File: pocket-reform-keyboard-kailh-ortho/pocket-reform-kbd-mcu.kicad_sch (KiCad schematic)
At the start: 177 parts, among them J1 Conn_01x06_Female, J2 USB, J3 UART, J4 AUX, SW65 SW_HWB, SW66 SW_RST, U1 SN74LV1T34DCK, U2 RP2040, U3 W25Q32JVSS, U4 MCP1700-3302E_SOT23, Y1 12MHz 18pF

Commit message: pocket keyboard 1.1 schematic and pcb mostly done
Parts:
- removed C15, C16, C17, C18, C19, C20, C21, C22, C23, C24, C25, C26, C27, C28, C29, C30, C31, C32, C33, C34, C35, C36, C37, C38, C39, C40, C41, C42, C43, C44, C45, C46, C47, C48, C49, C50, C51, C52, C53, C54, C55, C56, C57, C58, C59, C60, C61, C62, C63, C64, C65, C66, C67, C68, C69, C70, C71, C72, C73, C74, C76, C77, C78, C79: 0.1uF, Capacitor_SMD:C_0603_1608Metric, symbol Device:C_Small
- removed D100, D101, D102, D103, D104, D105, D106, D107, D108, D109, D110, D111, D112, D113, D114, D115, D116, D117, D118, D119, D120, D125, D126, D127, D128, D62, D63, D64, D65, D66, D67, D68, D69, D70, D71, D72, D73, D74, D75, D76, D77, D78, D79, D80, D81, D82, D83, D84, D85, D86, D87, D88, D89, D90, D91, D92, D93, D94, D95, D96, D97, D98, D99: SK6805-EC15, footprints:SK6805-EC15, symbol pocket-reform-keyboard:SK6805-EC15
- removed D61: SK6805-EC15, footprints:SK6805-EC15, symbol LED:SK6805
- removed R8: DNP, Resistor_SMD:R_0603_1608Metric, symbol Device:R_Small
- removed TP1, TP2: TestPoint, TestPoint:TestPoint_Pad_D1.0mm, symbol Connector:TestPoint
- removed U1: SN74LV1T34DCK, Package_TO_SOT_SMD:SOT-353_SC-70-5, symbol Logic_LevelTranslator:SN74LV1T34DCK
- removed U4: MCP1700-3302E_SOT23, Package_TO_SOT_SMD:SOT-23, symbol Regulator_Linear:MCP1700-3302E_SOT23
- added C80, C82: 10uF, Capacitor_SMD:C_0603_1608Metric, symbol Device:C_Small
- added J61: UART, Connector_JST:JST_SH_SM04B-SRSS-TB_1x04-1MP_P1.00mm_Horizontal, symbol Connector_Generic:Conn_01x04
- C1, C10, C11, C14, C2, C3, C4, C5, C6, C8, C9: footprint Capacitor_SMD:C_0603_1608Metric -> Capacitor_SMD:C_0402_1005Metric
- C12, C13: value 27pF -> 15pF; footprint Capacitor_SMD:C_0603_1608Metric -> Capacitor_SMD:C_0402_1005Metric; LCSC C107045 -> (none); Manufacturer Yageo -> (none); Manufacturer_No CC0603JRNPO9BN270 -> (none)
- C7, C75: footprint Capacitor_SMD:C_0603_1608Metric -> Capacitor_SMD:C_0402_1005Metric; LCSC C14664 -> (none); Manufacturer Yageo -> (none); Manufacturer_No CC0603KRX5R8BB105 -> (none)
- R1, R2, R3, R4, R6, R7, R9: footprint Resistor_SMD:R_0603_1608Metric -> Resistor_SMD:R_0402_1005Metric
- R5: value 4.7k -> 1k; footprint Resistor_SMD:R_0603_1608Metric -> Resistor_SMD:R_0402_1005Metric; LCSC C105428 -> (none); Manufacturer_No RC0603FR-074K7L -> (none)
- Y1: value 12MHz 18pF -> 12MHz 12pF; LCSC C91749 -> C20625731; Manufacturer Seiko Epson -> Abracon; Manufacturer_No Q22FA23V0041800 -> ABM8-272-T3
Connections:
- net +1V1: now also C75.1
- net +3V3: now also C80.1, J61.1 (Pin_1)
- net +5V: now also C82.1; no longer C75.1
- net GND: now also C80.2, C82.2, J61.3 (Pin_3)
- net SWC: now also J61.2 (Pin_2)
- net SWD: now also J61.4 (Pin_4)
- no-connect marks 10 -> 9
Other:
- note added: "SWD Debug"
- note added: "changed to 1k!"
- note added: "close to VREG_IN"
- note added: "close to VREG_OUT"
- note removed: "DNP!"
- note removed: "TODO: LCSC: wrong pn! was 4k7"
- note removed: "TODO: check wakeup IRQs"
- moved on the sheet: C1, C10, C11, C12, C13, C14, C2, C3, C4, C5, C6, C7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

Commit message: PREF keyboard: V1.5-R1
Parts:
- added C83: 10uF, Capacitor_SMD:C_0603_1608Metric, symbol Device:C_Small
- added R61, R68: 10k, Resistor_SMD:R_0402_1005Metric, symbol Device:R_Small
- added U12: AP22815A, Package_TO_SOT_SMD:SOT-23-5, symbol reform2:AP22815
- C1, C10, C11, C14, C2, C3, C4, C5, C6, C8, C9: LCSC C14663 -> C1525; Manufacturer Yageo -> Samsung; Manufacturer_No CC0603JPX7R9BB104 -> CL05B104KO5NNNC
- C12, C13: LCSC (none) -> C161530; Manufacturer (none) -> Murata; Manufacturer_No (none) -> GRM1555C1H150FA01D
- C7, C75: LCSC (none) -> C52923; Manufacturer (none) -> Samsung; Manufacturer_No (none) -> CL05A105KA5NQNC
- C80, C82: LCSC (none) -> C19702; Manufacturer (none) -> Samsung; Manufacturer_No (none) -> CL10A106KP8NNNC
- GFX1, H1, H10, H2, H3, H4, H5, H6, H7, H8, H9: now not fitted
- GFX2: footprint footprints:mpre-keyboard-badge-r1 -> footprints:pref-keyboard15-badge; now not fitted
- R1, R2: LCSC C185346 -> C31439; Manufacturer Yageo -> Uni-Royal; Manufacturer_No RC0603FR-0727R4L -> 0402WGF274JTCE
- R3: LCSC C14676 -> C11702; Manufacturer Yageo -> Uni-Royal; Manufacturer_No RC0603JR-071KL -> 0402WGF1001TCE
- R4, R6: LCSC C99198 -> C25744; Manufacturer Yageo -> Uni-Royal; Manufacturer_No RC0603JR-0710KL -> 0402WGF1002TCE
- R5: LCSC (none) -> C11702; Manufacturer Yageo -> Uni-Royal; Manufacturer_No (none) -> 0402WGF1001TCE
- R7, R9: LCSC C105428 -> C25900; Manufacturer Yageo -> Uni-Royal; Manufacturer_No RC0603FR-074K7L -> 0402WGF4701TCE
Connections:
- net +5V: now also R68.2, U12.5 (IN)
- net GND: now also C83.2, R61.1, U12.2 (GND)
- net LED_PWR_EN: now reaches U2.37 (GPIO25)
- net LED_PWR_EN: now also R61.2, U12.4 (EN)
- new net: R68.1, U12.3 (FLG)
- new net LED_POWER: C83.1, U12.1 (OUT)
- no-connect marks 9 -> 8
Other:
- note added: "SOURCE"
- note added: "WARNING: do not use B version by accident (active low)"
- note added: "rated to 28V"

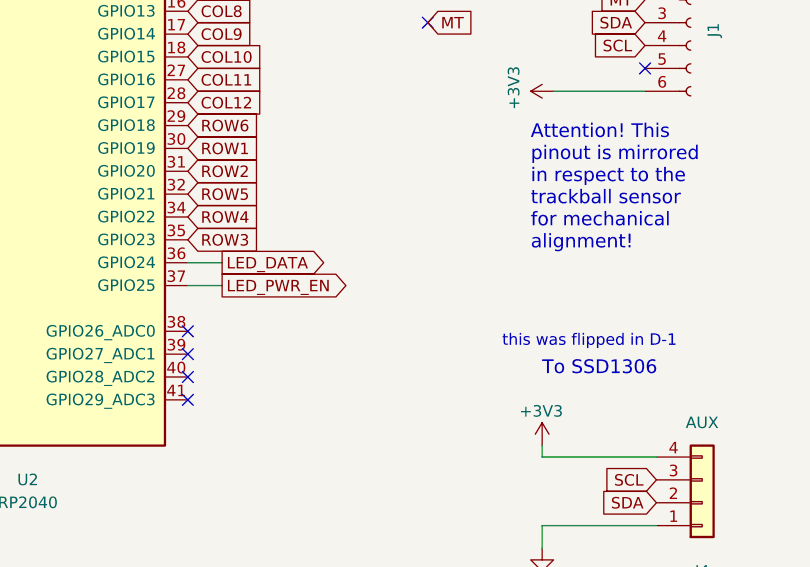
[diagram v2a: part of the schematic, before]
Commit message: kbd1.5: add note in schematic
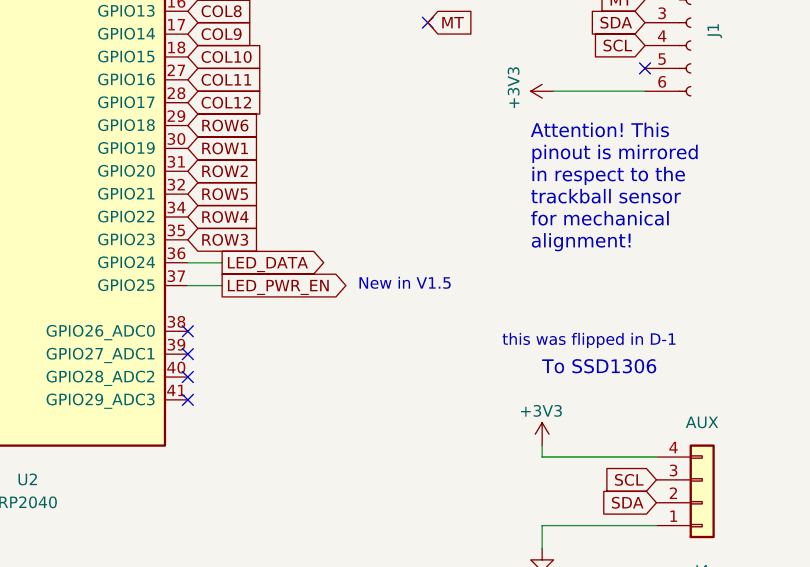
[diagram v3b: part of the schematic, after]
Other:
- note added: "New in V1.5"
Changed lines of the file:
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@@
+		)
+	)
+	(text "New in V1.5"
+		(exclude_from_sim no)
+		(at 142.24 138.43 0)
+		(effects
+			(font
+				(size 1.27 1.27)
+			)
 		)
 	)
